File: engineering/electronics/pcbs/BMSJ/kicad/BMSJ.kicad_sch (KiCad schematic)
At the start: 0 parts

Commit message: electronics: import Vector BMS as BMSJ
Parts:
- added C1, C17, C18, C19, C2, C20, C21, C25, C26, C48, C49, C5: 1u, Capacitor_SMD:C_0805_2012Metric, symbol Device:C
- added C10, C11, C12, C15, C16, C22, C23, C27, C28, C29, C3, C4, C42, C47, C55, C56, C57, C8, C9: 100n, Capacitor_SMD:C_0603_1608Metric, symbol Device:C
- added C13, C14, C6, C7: 100p, Capacitor_SMD:C_0603_1608Metric, symbol Device:C
- added C58, C59: 22u, Capacitor_SMD:C_0805_2012Metric, symbol BMS-Master-LV-rescue:C-Device-BMS-Master-rescue-BMS-Master-rescue
- added C60: 47n, Capacitor_SMD:C_0603_1608Metric, symbol BMS-Master-LV-rescue:C-Device-BMS-Master-rescue-BMS-Master-rescue
- added C61, C62, C63: 10u, Capacitor_SMD:C_0603_1608Metric, symbol BMS-Master-LV-rescue:C-Device-BMS-Master-rescue-BMS-Master-rescue
- added C64: 2.2u, Capacitor_SMD:C_0603_1608Metric, symbol BMS-Master-LV-rescue:C-Device-BMS-Master-rescue-BMS-Master-rescue
- added D1, D13, D14, D2: 1N4148W, Diode_SMD:D_SOD-123, symbol Diode:1N4148W
- added D15, D3: BZT52H-C62, Diode_SMD:D_SOD-123, symbol Diode:BZT52Bxx
- added D16, D4: LED, LED_SMD:LED_0603_1608Metric, symbol Device:LED
- added D22: POWER, LED_SMD:LED_0603_1608Metric, symbol BMS-Master-LV-rescue:LED-Device-BMS-Master-rescue-BMS-Master-rescue
- added D23: STATUS, LED_SMD:LED_0603_1608Metric, symbol BMS-Master-LV-rescue:LED-Device-BMS-Master-rescue-BMS-Master-rescue
- added D26, D27, D28: smcj150a, Diode_SMD:D_SMC, symbol Device:D_TVS
- added D29, D35: BZT52C16, Diodes_SMD:D_SOD-123, symbol Diode:BZT52Bxx
- added D30, D31, D32, D33, D34: 1N4148W, Diodes_SMD:D_SOD-123, symbol Diode:1N4148W
- added F1, F10, F11, F12, F13, F14, F15, F16, F17, F18, F19, F2, F20, F21, F22, F23, F24, F25, F26, F3, F4, F5, F6, F7, F8, F9: Fuse, symbol Device:Fuse
- added FB1, FB2: 33, Resistor_SMD:R_0603_1608Metric, symbol LTC6811-rescue:Ferrite_Bead-Device
- added J1: CT3151V1-0, Snapeda:CON4_CT3151V1-0_CTE, symbol Snapeda:CT3151V1-0
- added J10, J11, J13, J15, J27, J28, J29, J30, J31, J32, J33, J34, J35, J36, J37, J38, J39, J40, J41, J42, J5, J6, J7, J8: CT3151V1-2, Snapeda:CON4_CT3151V1-0_CTE, symbol Snapeda:CT3151V1-2
- added J16, J4: Temp, Connector_PinHeader_2.54mm:PinHeader_1x05_P2.54mm_Horizontal, symbol LTC6811-rescue:Conn_01x05_Male-Connector
- added J17: - Power +, Connector_Phoenix_MC_HighVoltage:PhoenixContact_MCV_1,5_2-G-5.08_1x02_P5.08mm_Vertical, symbol BMS-Master-LV-rescue:Conn_01x02-Connector_Generic-BMS-Master-rescue-BMS-Master-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
- added J18, J20, J21, J9: Conn_01x02_Pin, symbol Connector:Conn_01x02_Pin
- added J2: Charger +, Connector_Phoenix_MC_HighVoltage:PhoenixContact_MCV_1,5_2-G-5.08_1x02_P5.08mm_Vertical, symbol BMS-Master-LV-rescue:Conn_01x02-Connector_Generic-BMS-Master-rescue-BMS-Master-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
- added J23: Power Button, Connectors_Molex:Molex_KK-6410-05_05x2.54mm_Straight, symbol BMS-Master-LV-rescue:Conn_01x05-Connector_Generic-BMS-Master-rescue-BMS-Master-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
- added JP1, JP2: SolderJumper_2_Open, symbol Jumper:SolderJumper_2_Open
- added K1: HE3621A1200, Snapeda:KT12-1A-40L-THT_RELAY_KT12-1A-40L-THT, symbol Snapeda:KT12-1A-40L-THT
- added L1: 744043151, Inductors_SMD:L_Wuerth_WE-PD2-Typ-MS, symbol Device:L
- added LS1: CMT-8530S-SMT-TR, Samacsys:CMT8530SSMTTR, symbol Samacsys_kicad_sym:CMT-8530S-SMT-TR
- added PS1, PS2: RBM-0512S, Samacsys:RBM0512S, symbol Samacsys:RBM-0512S
- added Q1, Q2: NSV1C201MZ4, TO_SOT_Packages_SMD:SOT-223, symbol Device:Q_NPN_BCEC
- added Q16, Q22, Q23, Q24, Q25: BSS138, TO_SOT_Packages_SMD:SOT-23, symbol Transistor_FET:BSS138
- added Q18, Q19, Q20: IRFL4105PBF, Package_TO_SOT_SMD:SOT-223, symbol Device:Q_NMOS_GDSD
- added R1, R12, R13, R14, R15, R2, R5, R6, R78, R91, R93: 100, Resistor_SMD:R_0603_1608Metric, symbol Device:R
- added R10, R16, R17, R3: 1.2k, Resistor_SMD:R_0603_1608Metric, symbol Device:R
- added R100, R96, R98: 4.7M, Resistor_SMD:R_0603_1608Metric, symbol Device:R
- added R103: 10k, Resistor_SMD:R_0603_1608Metric, symbol Device:R
- added R104, R107, R108: 1, Resistor_SMD:R_0603_1608Metric, symbol BMS-Master-LV-rescue:R-Device-BMS-Master-rescue-BMS-Master-rescue
- added R105, R106: 4.7M, Resistor_SMD:R_0603_1608Metric, symbol BMS-Master-LV-rescue:R-Device-BMS-Master-rescue-BMS-Master-rescue
- added R109: 130k, Resistor_SMD:R_0603_1608Metric, symbol BMS-Master-LV-rescue:R-Device-BMS-Master-rescue-BMS-Master-rescue
- added R11, R22, R23, R24, R25, R26, R60, R61, R62, R63, R88: 100k, Resistor_SMD:R_0603_1608Metric, symbol Device:R
- added R110, R111, R114: 10k, Resistor_SMD:R_0603_1608Metric, symbol BMS-Master-LV-rescue:R-Device-BMS-Master-rescue-BMS-Master-rescue
- added R112: 100, Resistor_SMD:R_0603_1608Metric, symbol BMS-Master-LV-rescue:R-Device-BMS-Master-rescue-BMS-Master-rescue
- added R113: 1M, Resistor_SMD:R_0603_1608Metric, symbol BMS-Master-LV-rescue:R-Device-BMS-Master-rescue-BMS-Master-rescue
- added R125: 2K2, Resistor_SMD:R_0805_2012Metric_Pad1.20x1.40mm_HandSolder, symbol Device:R
- added R18, R4: 806, Resistor_SMD:R_0603_1608Metric, symbol Device:R
- added R19, R21, R8, R9: 0, Resistor_SMD:R_0603_1608Metric, symbol Device:R
- added R20, R7: 1M, Resistor_SMD:R_0603_1608Metric, symbol Device:R
- added R70: 270, symbol Device:R
- added R71, R75, R76: 470, Resistor_SMD:R_0603_1608Metric, symbol BMS-Master-LV-rescue:R-Device-BMS-Master-rescue-BMS-Master-rescue
- added R72, R73: 220k, Resistor_SMD:R_2512_6332Metric, symbol Device:R
- added R74, R89, R90: 4.75k, Resistor_SMD:R_0603_1608Metric, symbol Device:R
- added R77: 1.5k, Resistor_SMD:R_0603_1608Metric, symbol BMS-Master-LV-rescue:R-Device-BMS-Master-rescue-BMS-Master-rescue
- added R92: WSLP5931L1000FEA, Resistor_SMD:R_5931_15076Metric, symbol Device:R
- added R94: 100k, Resistor_SMD:R_2512_6332Metric, symbol Device:R
- added R95, R97, R99: 10, Resistor_SMD:R_0603_1608Metric, symbol Device:R
- added TH1, TH2: 100k, Resistor_SMD:R_0805_2012Metric, symbol Device:Thermistor
- added TH3: Thermistor_NTC 100k, Resistor_SMD:R_0805_2012Metric, symbol Device:Thermistor_NTC
- added U1, U2: LTC6811-1, Housings_SSOP:TSSOP-48_6.1x12.5mm_Pitch0.5mm, symbol ENNOID:LTC6811-1
- added U5: LM5165YDRC, Housings_SON:Texas_S-PVSON-N10_ThermalVias, symbol Regulator_Switching:LM5165
- added U7: INA226, Package_SO:VSSOP-10_3x3mm_P0.5mm, symbol BMS-Master-LV-rescue:INA226-Analog_ADC
- added U8: SFH617A-2X009T, Housings_DIP:SMDIP-4_W9.53mm_Clearance8mm, symbol Isolator:SFH617A-2X009T
- added U9: CPC1019N, Samacsys:SOP254P610X218-4N, symbol Samacsys_kicad_sym:CPC1019N
- added XMER1, XMER2: HM2102NL, Snapeda:HM2102NL_PUL, symbol Snapeda:HM2102NL
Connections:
- new net: C7.1, XMER1.11
- new net: XMER1.4, XMER2.1
- new net: XMER1.6, XMER2.3
- new net: C6.1, XMER1.8
- new net: R3.1, U1.45 (IBIAS)
- new net: R3.2, R4.1, U1.46 (ICMP)
- new net: F1.1, F26.1, J30.1
- new net: F2.1, J29.1
- new net: F3.1, J28.1
- new net: F4.1, J27.1
- new net: F5.1, J15.1
- new net: F6.1, J13.1
- new net: F7.1, J11.1
- new net: F8.1, J10.1
- new net: F9.1, J8.1
- new net: F10.1, J7.1
- new net: F11.1, J6.1
- new net: F12.1, J5.1
- new net: Q1.1 (B), U1.38 (DRIVE)
- new net: PS1.6 (+VOUT_), Q1.2 (C), Q1.4 (C)
- new net: C2.1, U1.35 (Vref1)
- new net: D13.1 (K), D14.1 (K), D15.1 (K), FB1.1, R1.1, R2.1
- new net: C3.1, R2.2, U1.1 (V+)
- new net: F13.1, J1.1
- new net: C4.1, R1.2
- new net: R9.1, U1.36 (DTEN)
- new net: R7.1, U1.39 (WDT)
- new net: R8.1, U1.40 (ISOMD)
- new net: D16.1 (K), R10.1
- new net: K1.COM, R70.2
- new net: D4.1 (K), R16.1
- new net: C64.1, D35.1 (K), Q24.1 (G), R111.1, R112.2, R113.1
- new net: C64.2, D33.1 (K), R113.2
- new net: Q19.1 (G), R97.1, R98.2
- new net: F18.1, J35.1
- new net: L1.1, U5.1 (SW)
- new net: L1.2, R104.1, R107.1, R108.1, U5.8 (FB)
- new net: D32.1 (K), R111.2
- new net: LS1.2 (-), Q16.3 (D)
- new net: R21.1, U2.36 (DTEN)
- new net: D29.1 (K), D30.2 (A), D33.2 (A), D34.2 (A), Q23.1 (G), Q25.3 (D), R105.1
- new net: C47.1, R72.2, R88.1, U7.8 (Vbus)
- new net: F23.1, J40.1
- new net: D1.1 (K), D2.1 (K), D3.1 (K), FB2.1, R13.1, R14.1
- new net: C61.2, R107.2
- new net: Q20.1 (G), R100.2, R99.1
- new net: R94.1, U8.1
- new net: C18.1, U2.35 (Vref1)
- new net: F21.1, J38.1
- new net: F25.1, J42.1
- new net: Q18.1 (G), R95.1, R96.2
- new net: R91.2, R92.2
- new net: C16.1, R13.2
- new net: F22.1, J39.1
- new net: D23.2 (A), R76.1
- new net: C60.2, U5.4 (SS)
- new net: R109.2, U5.5 (RT)
- new net: Q23.3 (D), R106.1, U5.7 (EN)
- new net: JP1.1 (A), XMER2.6
- new net: JP1.2 (B), R78.1
- new net: F15.1, J32.1
- new net: F24.1, J41.1
- new net: R125.2, U9.1 (+CONTROL)
- new net: F20.1, J37.1
- new net: D22.2 (A), R75.1
- new net: J23.4 (Pin_4), R71.1
- new net: C56.2, R91.1, U7.10 (Vin+)
- new net: J20.2 (Pin_2), U9.3 (LOAD_1)
- new net: J20.1 (Pin_1), U9.4 (LOAD_2)
- new net: C57.2, R93.1, U7.9 (Vin-)
- new net: JP2.1 (A), XMER2.4
- new net: JP2.2 (B), R78.2
- new net: F16.1, J33.1
- new net: J2.2 (Pin_2), R94.2
- new net: D31.1 (K), R110.1
- new net: PS2.6 (+VOUT_), Q2.2 (C), Q2.4 (C)
- new net: C13.1, XMER2.8
- new net: F14.1, J31.1
- new net: F19.1, J36.1
- new net: C62.2, R108.2
- new net: Q2.1 (B), U2.38 (DRIVE)
- new net: C15.1, R14.2, U2.1 (V+)
- new net: R19.1, U2.40 (ISOMD)
- new net: C14.1, XMER2.11
- new net: R20.1, U2.39 (WDT)
- new net: R17.1, U2.45 (IBIAS)
- new net: R17.2, R18.1, U2.46 (ICMP)
- new net: F17.1, J34.1
- new net +12V: C58.2, C59.2, J18.1 (Pin_1), J21.1 (Pin_1), J9.1 (Pin_1), K1.COIL1, R105.2, R106.2, U5.2 (VIN)
- new net +3.3V: C42.2, R103.1, R89.1, R90.1, U7.6 (VS)
- new net +3V3: C63.2, D31.2 (A), D32.2 (A), J23.3 (Pin_3), LS1.1 (+), R104.2, R75.2
- new net +5V_Supply: C48.2, C49.2, PS1.1 (+VIN), PS2.1 (+VIN)
- new net BAT+: D26.1 (A1), D27.1 (A1), D28.1 (A1), J17.1 (Pin_1), J2.1 (Pin_1), K1.NO, R70.1, R72.1, R73.1
- new net Charge: J18.2 (Pin_2), Q20.2 (D), Q20.4 (D)
- new net ChargeDetect: D34.1 (K), R110.2, U8.4
- new net ChargeEnable: R99.2
- new net Cooling: J9.2 (Pin_2), Q18.2 (D), Q18.4 (D)
- new net CoolingEnable: R95.2
- new net DischargeEnable: Q22.3 (D), R125.1
- new net EnableFromExt: D30.1 (K)
- new net GND: C42.1, C47.2, C55.2, C56.1, C57.1, C58.1, C59.1, C60.1, C61.1, C62.1, C63.1, D22.1 (K), D23.1 (K), D26.2 (A2), D27.2 (A2), D28.2 (A2), D29.2 (A), D35.2 (A), J17.2 (Pin_2), J21.2 (Pin_2), J23.1 (Pin_1), J23.5 (Pin_5), Q16.1 (G), Q16.2 (S), Q18.3 (S), Q19.3 (S), Q20.3 (S), Q22.2 (S), Q23.2 (S), Q24.2 (S), Q25.2 (S), R100.1, R109.1, R114.2, R74.2, R77.1, R77.2, R88.2, R92.1, R93.2, R96.1, R98.1, TH3.1, U5.10 (GND), U5.11 (PAD), U5.3 (ILIM), U7.7 (GND), U8.2, U8.3, U9.2 (-CONTROL)
- new net GND1: C1.2, C10.2, C11.2, C12.2, C2.2, C25.2, C26.2, C3.2, C4.2, C5.2, C6.2, C7.2, C8.2, C9.2, D13.2 (A), D14.2 (A), D15.2 (A), F13.2, J4.1 (Pin_1), PS1.5 (-VOUT_), R10.2, R4.2, R9.2, TH1.2, U1.26 (C0), U1.30 (V-**), U1.31 (V-)
- new net GND2: C13.2, C14.2, C15.2, C16.2, C17.2, C18.2, C19.2, C20.2, C21.2, C22.2, C23.2, C27.2, C28.2, C29.2, D1.2 (A), D2.2 (A), D3.2 (A), F26.2, J16.1 (Pin_1), PS2.5 (-VOUT_), R16.2, R18.2, R21.2, TH2.2, U2.26 (C0), U2.30 (V-**), U2.31 (V-)
- new net GND_5V_Supply: C48.1, C49.1, PS1.2 (-VIN), PS2.2 (-VIN)
- new net IMA_1: R6.2, U1.41 (IMA), XMER1.12
- new net IMA_2: R15.2, U2.41 (IMA), XMER2.12
- new net IMB_1: R5.2, U1.47 (IMB), XMER1.9
- new net IMB_2: R12.2, U2.47 (IMB), XMER2.9
- new net IPA_1: R6.1, U1.42 (IPA), XMER1.10
- new net IPA_2: R15.1, U2.42 (IPA), XMER2.10
- new net IPB_1: R5.1, U1.48 (IPB), XMER1.7
- new net IPB_2: R12.1, U2.48 (IPB), XMER2.7
- new net MCU/LED0: R76.2
- new net MCU/MA: XMER1.1
- new net MCU/PA: XMER1.3
- new net MCU/PowerLED: R71.2
- new net NTC_Switch: TH3.2
- new net PowerButton: J23.2 (Pin_2), Q24.3 (D)
- new net PowerEnable: Q25.1 (G), R114.1
- new net Precharge: K1.COIL2, Q19.2 (D), Q19.4 (D)
- new net PrechargeEnable: R97.2
- new net PushButton: R112.1
- new net SCL: R89.2, U7.5 (SCL)
- new net SDA: R90.2, U7.4 (SDA)
- new net Safety: Q22.1 (G), R103.2
- new net T1_1: C12.1, R11.2, TH1.1, U1.27 (GPIO1)
- new net T1_2: C22.1, R26.2, TH2.1, U2.27 (GPIO1)
- new net T2: C23.1, C8.1, J16.2 (Pin_2), J4.2 (Pin_2), R22.1, R60.1
- new net T2_1: U1.28 (GPIO2)
- new net T2_2: U2.28 (GPIO2)
- new net T3: C27.1, C9.1, J16.3 (Pin_3), J4.3 (Pin_3), R23.1, R61.1
- new net T3_1: U1.29 (GPIO3)
- new net T3_2: U2.29 (GPIO3)
- new net T4: C10.1, C28.1, J16.4 (Pin_4), J4.4 (Pin_4), R24.1, R62.1
- new net T4_1: U1.32 (GPIO4)
- new net T4_2: U2.32 (GPIO4)
- new net T5: C11.1, C29.1, J16.5 (Pin_5), J4.5 (Pin_5), R25.1, R63.1
- new net T5_1: U1.33 (GPIO5)
- new net T5_2: U2.33 (GPIO5)
- new net Vpack: C55.1, R73.2, R74.1
- new net Vref2_1: C1.1, R11.1, R60.2, R61.2, R62.2, R63.2, U1.34 (Vref2)
- new net Vref2_2: C17.1, R22.2, R23.2, R24.2, R25.2, R26.1, U2.34 (Vref2)
- new net Vreg_1: C25.1, C26.1, C5.1, D16.2 (A), Q1.3 (E), R7.2, R8.2, U1.37 (Vreg)
- new net Vreg_2: C19.1, C20.1, C21.1, D4.2 (A), Q2.3 (E), R19.2, R20.2, U2.37 (Vreg)
- new net cell10_1/C: U1.6 (C10)
- new net cell10_1/C+: F3.2
- new net cell10_1/C-: F4.2
- new net cell10_1/CM: U1.8 (C9)
- new net cell10_1/S: U1.7 (S10)
- new net cell10_2/C: U2.6 (C10)
- new net cell10_2/C+: F16.2
- new net cell10_2/C-: F17.2
- new net cell10_2/CM: U2.8 (C9)
- new net cell10_2/S: U2.7 (S10)
- new net cell11_1/C: U1.4 (C11)
- new net cell11_1/C+: F2.2
- new net cell11_1/S: U1.5 (S11)
- new net cell11_2/C: U2.4 (C11)
- new net cell11_2/C+: F15.2
- new net cell11_2/S: U2.5 (S11)
- new net cell12_1/C: U1.2 (C12)
- new net cell12_1/C+: F1.2, FB1.2
- new net cell12_1/S: U1.3 (S12)
- new net cell12_2/C: U2.2 (C12)
- new net cell12_2/C+: F14.2, FB2.2
- new net cell12_2/S: U2.3 (S12)
- new net cell1_1/C: U1.24 (C1)
- new net cell1_1/C+: F12.2
- new net cell1_1/S: U1.25 (S1)
- new net cell1_2/C: U2.24 (C1)
- new net cell1_2/C+: F25.2
- new net cell1_2/S: U2.25 (S1)
- new net cell2_1/C: U1.22 (C2)
- new net cell2_1/C+: F11.2
- new net cell2_1/S: U1.23 (S2)
- new net cell2_2/C: U2.22 (C2)
- new net cell2_2/C+: F24.2
- new net cell2_2/S: U2.23 (S2)
- new net cell3_1/C: U1.20 (C3)
- new net cell3_1/C+: F10.2
- new net cell3_1/S: U1.21 (S3)
- new net cell3_2/C: U2.20 (C3)
- new net cell3_2/C+: F23.2
- new net cell3_2/S: U2.21 (S3)
- new net cell4_1/C: U1.18 (C4)
- new net cell4_1/C+: F9.2
- new net cell4_1/S: U1.19 (S4)
- new net cell4_2/C: U2.18 (C4)
- new net cell4_2/C+: F22.2
- new net cell4_2/S: U2.19 (S4)
- new net cell5_1/C: U1.16 (C5)
- new net cell5_1/C+: F8.2
- new net cell5_1/S: U1.17 (S5)
- new net cell5_2/C: U2.16 (C5)
- new net cell5_2/C+: F21.2
- new net cell5_2/S: U2.17 (S5)
- new net cell6_1/C: U1.14 (C6)
- new net cell6_1/C+: F7.2
- new net cell6_1/S: U1.15 (S6)
- new net cell6_2/C: U2.14 (C6)
- new net cell6_2/C+: F20.2
- new net cell6_2/S: U2.15 (S6)
- new net cell7_1/C: U1.12 (C7)
- new net cell7_1/C+: F6.2
- new net cell7_1/S: U1.13 (S7)
- new net cell7_2/C: U2.12 (C7)
- new net cell7_2/C+: F19.2
- new net cell7_2/S: U2.13 (S7)
- new net cell8_1/C: U1.10 (C8)
- new net cell8_1/C+: F5.2
- new net cell8_1/S: U1.11 (S8)
- new net cell8_2/C: U2.10 (C8)
- new net cell8_2/C+: F18.2
- new net cell8_2/S: U2.11 (S8)
- new net cell9_1/S: U1.9 (S9)
- new net cell9_2/S: U2.9 (S9)
- no-connect marks 0 -> 15
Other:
- added sheet MCU (MCU.kicad_sch)
- added sheet cell10_1 (cell.kicad_sch)
- added sheet cell10_2 (cell2.kicad_sch)
- added sheet cell11_1 (cell.kicad_sch)
- added sheet cell11_2 (cell2.kicad_sch)
- added sheet cell12_1 (cell.kicad_sch)
- added sheet cell12_2 (cell2.kicad_sch)
- added sheet cell1_1 (cell.kicad_sch)
- added sheet cell1_2 (cell2.kicad_sch)
- added sheet cell2_1 (cell.kicad_sch)
- added sheet cell2_2 (cell2.kicad_sch)
- added sheet cell3_1 (cell.kicad_sch)
- added sheet cell3_2 (cell2.kicad_sch)
- added sheet cell4_1 (cell.kicad_sch)
- added sheet cell4_2 (cell2.kicad_sch)
- added sheet cell5_1 (cell.kicad_sch)
- added sheet cell5_2 (cell2.kicad_sch)
- added sheet cell6_1 (cell.kicad_sch)
- added sheet cell6_2 (cell2.kicad_sch)
- added sheet cell7_1 (cell.kicad_sch)
- added sheet cell7_2 (cell2.kicad_sch)
- added sheet cell8_1 (cell.kicad_sch)
- added sheet cell8_2 (cell2.kicad_sch)
- added sheet cell9_1 (cell.kicad_sch)
- added sheet cell9_2 (cell2.kicad_sch)
- note added: "0.1mOhm"
- note added: "BUZZER"
- note added: "C1+"
- note added: "C1-"
- note added: "C10+"
- note added: "C11+"
- note added: "C12+"
- note added: "C13+"
- note added: "C14+"
- note added: "C15+"
- note added: "C16+"
- note added: "C17+"
- note added: "C18+"
- note added: "C19+"
- note added: "C2+"
- note added: "C20+"
- note added: "C21+"
- note added: "C22+"
- note added: "C23+"
- note added: "C24+"
- note added: "C3+"
- note added: "C4+"
- note added: "C5+"
- note added: "C6+"
- note added: "C7+"
- note added: "C8+"
- note added: "C9+"
- note added: "For future mosfet control"
- note added: "ISOLATED"
- note added: "Mosfets for main power"
- note added: "Precharge"
- company: Arrow -> (none)
- title: BMSJ -> (none)
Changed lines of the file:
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@@
-(kicad_sch
-    (version 20231120)
-    (generator "project-longshot")
-    (generator_version "0.1")
-    (paper "A4")
-    (title_block
-        (title "BMSJ")
-        (company "Arrow")
-    )
-)

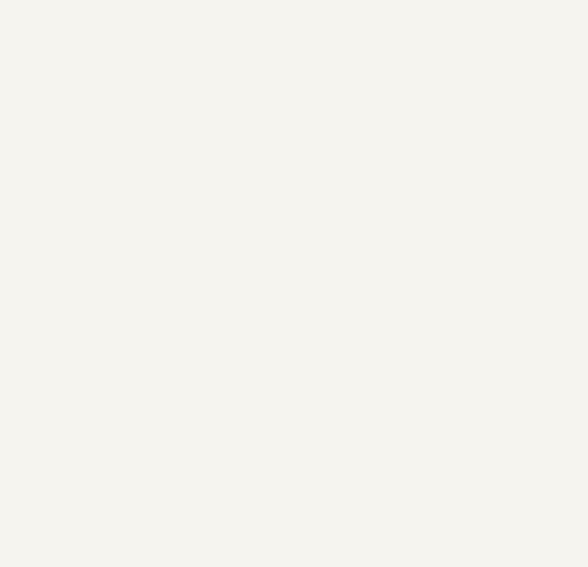
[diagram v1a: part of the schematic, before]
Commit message: Kicad_Update
- Add busbar cell connection
- Screw holes
- Edge cuts
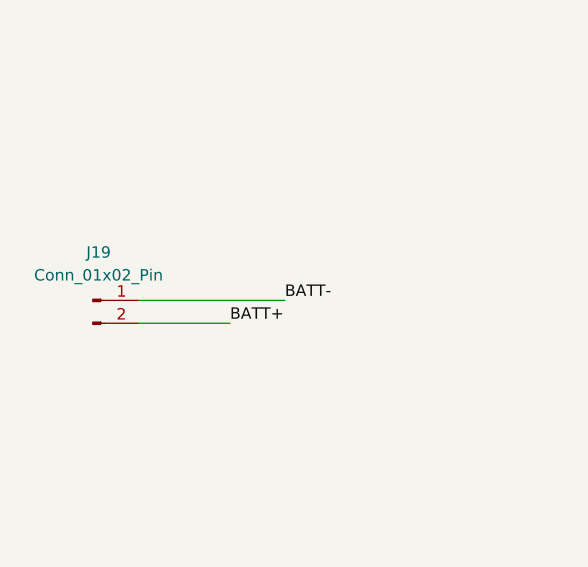
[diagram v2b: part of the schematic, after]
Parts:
- added J19: Conn_01x02_Pin, symbol Connector:Conn_01x02_Pin
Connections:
- new net BATT+: J19.2 (Pin_2)
- new net BATT-: J19.1 (Pin_1)

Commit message: KiCad_Update
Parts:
- removed J19: Conn_01x02_Pin, symbol Connector:Conn_01x02_Pin
- added J35: ET60S-D06-0-00-D06-X-V1-S, BMSJ:SAMTEC_ET60S-D06-0-00-D06-X-V1-S, symbol BMSJ:ET60S-D06-0-00-D06-X-V1-S
- renumbered C6 to C1, C26 to C10, C8 to C11, C9 to C12, C10 to C13, C11 to C14, C42 to C15, C47 to C16, C55 to C17, C12 to C18, C56 to C19, C7 to C2, C57 to C20, C13 to C21, C14 to C22, C58 to C23, C59 to C24, C15 to C25, C16 to C26, C49 to C27, C60 to C28, C61 to C29, C62 to C30, C63 to C31, C17 to C32, C18 to C33, C19 to C34, C20 to C35, C21 to C36, C64 to C37, C23 to C38, C27 to C39, C28 to C40, C29 to C41, C22 to C42, C48 to C5, C1 to C6, C2 to C7, C5 to C8, C25 to C9, D13 to D1, D3 to D10, D29 to D11, D30 to D12, D31 to D13, D32 to D14, D33 to D15, D34 to D16, D4 to D17, D35 to D18, D22 to D19, D14 to D2, D23 to D20, D15 to D3, D26 to D4, D27 to D5, D28 to D6, D16 to D7, D1 to D8, D2 to D9, J17 to J1, J8 to J11, J7 to J12, J6 to J13, J5 to J14, J18 to J15, J1 to J16, J4 to J17, J20 to J18, J2 to J19, J9 to J2, J31 to J20, J32 to J21, J33 to J22, J34 to J23, J35 to J24, J36 to J25, J37 to J26, J38 to J27, J39 to J28, J40 to J29, J30 to J3, J41 to J30, J42 to J31, J16 to J32, J21 to J33, J23 to J34, J29 to J4, J28 to J5, J27 to J6, J15 to J7, J13 to J8, J11 to J9, Q18 to Q1, Q16 to Q10, Q1 to Q2, Q19 to Q3, Q20 to Q4, Q22 to Q5, Q23 to Q6, Q2 to Q7, Q24 to Q8, Q25 to Q9, R8 to R10, R7 to R11, R9 to R12, R97 to R13, R98 to R14, R60 to R15, R61 to R16, R62 to R17, R63 to R18, R99 to R19, R100 to R20, R72 to R21, R125 to R22, R73 to R23, R74 to R24, R88 to R25, R11 to R26, R89 to R27, R90 to R28, R103 to R29, R5 to R3, R91 to R30, R10 to R31, R92 to R32, R93 to R33, R94 to R34, R13 to R35, R14 to R36, R12 to R37, R78 to R38, R15 to R39, R6 to R4, R104 to R40, R105 to R41, R106 to R42, R107 to R43, R108 to R44, R109 to R45, R17 to R46, R18 to R47, R19 to R48, R20 to R49, R70 to R5, R21 to R50, R22 to R51, R23 to R52, R24 to R53, R25 to R54, R110 to R55, R111 to R56, R112 to R57, R113 to R58, R26 to R59, R3 to R6, R16 to R60, R114 to R61, R71 to R62, R75 to R63, R76 to R64, R77 to R65, R4 to R7, R95 to R8, R96 to R9, TH3 to TH2, TH2 to TH3, U9 to U2, U7 to U3, U8 to U4, U2 to U6
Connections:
- net BATT+: now also J35.P08_1 (P08), J35.P08_2 (P08__1), J35.P08_3 (P08__2), J35.P08_4 (P08__3), J35.P08_5 (P08__4), J35.P08_6 (P08__5), J35.P08_7 (P08__6), J35.P08_8 (P08__7), J35.P09_1 (P09), J35.P09_2 (P09__1), J35.P09_3 (P09__2), J35.P09_4 (P09__3), J35.P09_5 (P09__4), J35.P09_6 (P09__5), J35.P09_7 (P09__6), J35.P09_8 (P09__7), J35.P10_1 (P10), J35.P10_2 (P10__1), J35.P10_3 (P10__2), J35.P10_4 (P10__3), J35.P10_5 (P10__4), J35.P10_6 (P10__5), J35.P10_7 (P10__6), J35.P10_8 (P10__7), J35.P11_1 (P11), J35.P11_2 (P11__1), J35.P11_3 (P11__2), J35.P11_4 (P11__3), J35.P11_5 (P11__4), J35.P11_6 (P11__5), J35.P11_7 (P11__6), J35.P11_8 (P11__7), J35.P12_1 (P12), J35.P12_2 (P12__1), J35.P12_3 (P12__2), J35.P12_4 (P12__3), J35.P12_5 (P12__4), J35.P12_6 (P12__5), J35.P12_7 (P12__6), J35.P12_8 (P12__7)
- net BATT-: now also J35.P01_1 (P01), J35.P01_2 (P01__1), J35.P01_3 (P01__2), J35.P01_4 (P01__3), J35.P01_5 (P01__4), J35.P01_6 (P01__5), J35.P01_7 (P01__6), J35.P01_8 (P01__7), J35.P02_1 (P02), J35.P02_2 (P02__1), J35.P02_3 (P02__2), J35.P02_4 (P02__3), J35.P02_5 (P02__4), J35.P02_6 (P02__5), J35.P02_7 (P02__6), J35.P02_8 (P02__7), J35.P03_1 (P03), J35.P03_2 (P03__1), J35.P03_3 (P03__2), J35.P03_4 (P03__3), J35.P03_5 (P03__4), J35.P03_6 (P03__5), J35.P03_7 (P03__6), J35.P03_8 (P03__7), J35.P04_1 (P04), J35.P04_2 (P04__1), J35.P04_3 (P04__2), J35.P04_4 (P04__3), J35.P04_5 (P04__4), J35.P04_6 (P04__5), J35.P04_7 (P04__6), J35.P04_8 (P04__7), J35.P05_1 (P05), J35.P05_2 (P05__1), J35.P05_3 (P05__2), J35.P05_4 (P05__3), J35.P05_5 (P05__4), J35.P05_6 (P05__5), J35.P05_7 (P05__6), J35.P05_8 (P05__7)
- new net BCAN_H: J35.P07_1 (P07), J35.P07_2 (P07__1), J35.P07_3 (P07__2), J35.P07_4 (P07__3), J35.P07_5 (P07__4), J35.P07_6 (P07__5), J35.P07_7 (P07__6), J35.P07_8 (P07__7)
- new net BCAN_L: J35.P06_1 (P06), J35.P06_2 (P06__1), J35.P06_3 (P06__2), J35.P06_4 (P06__3), J35.P06_5 (P06__4), J35.P06_6 (P06__5), J35.P06_7 (P06__6), J35.P06_8 (P06__7)
